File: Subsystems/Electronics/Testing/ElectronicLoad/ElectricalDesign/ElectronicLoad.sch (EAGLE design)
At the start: 74 parts, among them J1 USB, J2 Current Input, J3 Current Sense, J4 Voltage Sense, J5 SWD, Q1 IRFP4368PBF, Q2 SiRA20DP, Q3 SiRA20DP, Q4 IRFP4368PBF, SW1 Nice Knob, SW2 Nice Button, U1 STM32L476RGT, U2 AD8515, U3 FT230XQ, U4 INA199C1, U6 INA199C1, Y1 8MHz ±10ppm

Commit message: Update ElectronicLoad.sch
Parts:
- J6: value (none) -> FAN
- J7: value (none) -> 12 V Input
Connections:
- removed net N$2: U1A.PA11
- net FAN_SENSE: now also U1A.PA11
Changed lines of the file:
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@@
 <part name="SUPPLY56" library="CougsInSpace-PowerSymbols" deviceset="5.0V" device=""/>
 <part name="OFFSHEET11" library="CougsInSpace-Aesthetics" deviceset="OFF_SHEET-OUT" device=""/>
-<part name="J6" library="CougsInSpace-Connectors" deviceset="1X04" device="THT2.54-1X04-LOCK"/>
+<part name="J6" library="CougsInSpace-Connectors" deviceset="1X04" device="THT2.54-1X04-LOCK" value="FAN"/>
 <part name="OFFSHEET47" library="CougsInSpace-Aesthetics" deviceset="OFF_SHEET-OUT" device=""/>
 <part name="OFFSHEET49" library="CougsInSpace-Aesthetics" deviceset="OFF_SHEET-IN" device=""/>
@@
 <part name="SUPPLY67" library="CougsInSpace-PowerSymbols" deviceset="PGND" device=""/>
 <part name="OFFSHEET51" library="CougsInSpace-Aesthetics" deviceset="OFF_SHEET-OUT" device=""/>
-<part name="J7" library="CougsInSpace-Connectors" deviceset="BARREL" device="-2.1X5.5-R"/>
+<part name="J7" library="CougsInSpace-Connectors" deviceset="BARREL" device="-2.1X5.5-R" value="12 V Input"/>
 <part name="SUPPLY68" library="CougsInSpace-PowerSymbols" deviceset="12.0V" device=""/>
 <part name="SUPPLY69" library="CougsInSpace-PowerSymbols" deviceset="PGND" device=""/>
@@
 </segment>
 </net>
-<net name="N$2" class="0">
-<segment>
-<pinref part="U1" gate="A" pin="PA11"/>
-<wire x1="33.02" y1="66.04" x2="50.8" y2="66.04" width="0.1524" layer="91"/>
-</segment>
-</net>
-<net name="FAN_SENSE" class="0">
-<segment>
-<wire x1="38.1" y1="66.04" x2="55.88" y2="66.04" width="0.1524" layer="91"/>
-<label x="35.56" y="66.04" size="1.778" layer="95"/>
-<label x="35.56" y="66.04" size="1.778" layer="95"/>
-</segment>
-</net>
 <net name="FAN_CONTROL" class="0">
 <segment>
@@
 <pinref part="J7" gate="G$1" pin="CENTER"/>
 <wire x1="172.72" y1="165.1" x2="167.64" y2="165.1" width="0.1524" layer="91"/>
+</segment>
+</net>
+<net name="FAN_SENSE" class="0">
+<segment>
+<pinref part="U1" gate="A" pin="PA11"/>
+<wire x1="33.02" y1="66.04" x2="55.88" y2="66.04" width="0.1524" layer="91"/>
+<label x="35.56" y="66.04" size="1.778" layer="95"/>
 </segment>
 </net>
@@
 </instance>
 <instance part="OFFSHEET16" gate="G$1" x="83.82" y="55.88" smashed="yes" rot="MR0"/>
-<instance part="OFFSHEET24" gate="G$1" x="210.82" y="48.26" smashed="yes" rot="MR0"/>
+<instance part="OFFSHEET24" gate="G$1" x="106.68" y="132.08" smashed="yes" rot="MR0"/>
 <instance part="J2" gate="G$1" x="144.78" y="142.24" smashed="yes">
 <attribute name="VALUE" x="145.415" y="138.43" size="1.778" layer="96" align="center"/>
@@
 <instance part="OFFSHEET49" gate="G$1" x="104.14" y="157.48" smashed="yes" rot="MR0"/>
 <instance part="OFFSHEET50" gate="G$1" x="104.14" y="154.94" smashed="yes" rot="MR0"/>
-<instance part="SUPPLY66" gate="G$1" x="96.52" y="162.56" smashed="yes">
-<attribute name="VALUE" x="96.52" y="166.116" size="1.27" layer="96" align="center"/>
-</instance>
-<instance part="SUPPLY67" gate="G$1" x="91.44" y="162.56" smashed="yes" rot="R90"/>
+<instance part="SUPPLY66" gate="G$1" x="88.9" y="162.56" smashed="yes">
+<attribute name="VALUE" x="88.9" y="166.116" size="1.27" layer="96" align="center"/>
+</instance>
+<instance part="SUPPLY67" gate="G$1" x="86.36" y="149.86" smashed="yes"/>
 </instances>
 <busses>
@@
 </segment>
 </net>
+<net name="12.0V" class="0">
+<segment>
+<pinref part="J6" gate="G$1" pin="2"/>
+<wire x1="81.28" y1="160.02" x2="88.9" y2="160.02" width="0.1524" layer="91"/>
+<pinref part="SUPPLY66" gate="G$1" pin="12.0V"/>
+<wire x1="88.9" y1="160.02" x2="88.9" y2="162.56" width="0.1524" layer="91"/>
+</segment>
+</net>
 <net name="FAN_SENSE" class="0">
 <segment>
@@
 </segment>
 </net>
-<net name="FAN_SENSE1" class="0">
-<segment>
-<wire x1="81.28" y1="154.94" x2="101.6" y2="154.94" width="0.1524" layer="91"/>
-</segment>
-</net>
 <net name="PGND" class="0">
 <segment>
 <pinref part="J6" gate="G$1" pin="1"/>
+<wire x1="81.28" y1="162.56" x2="86.36" y2="162.56" width="0.1524" layer="91"/>
 <pinref part="SUPPLY67" gate="G$1" pin="PGND"/>
-<wire x1="88.9" y1="162.56" x2="81.28" y2="162.56" width="0.1524" layer="91"/>
-</segment>
-</net>
-<net name="12.0V" class="0">
-<segment>
-<pinref part="J6" gate="G$1" pin="2"/>
-<wire x1="81.28" y1="160.02" x2="96.52" y2="160.02" width="0.1524" layer="91"/>
-<pinref part="SUPPLY66" gate="G$1" pin="12.0V"/>
-<wire x1="96.52" y1="160.02" x2="96.52" y2="162.56" width="0.1524" layer="91"/>
-</segment>
-</net>
+<wire x1="86.36" y1="162.56" x2="86.36" y2="152.4" width="0.1524" layer="91"/>
+</segment>
+</net>

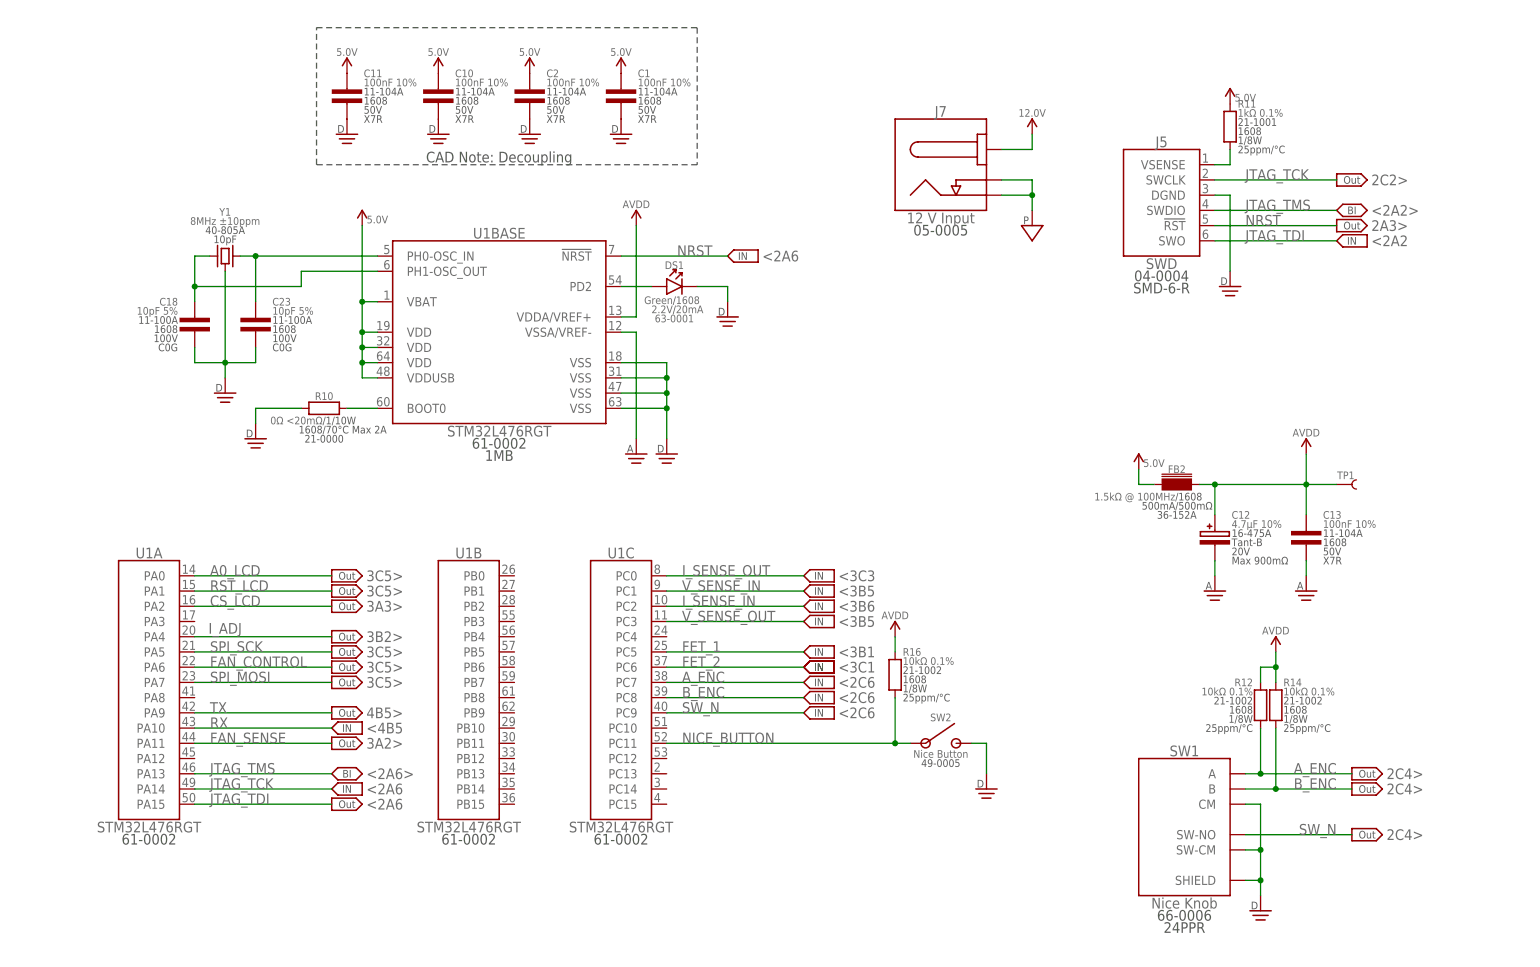
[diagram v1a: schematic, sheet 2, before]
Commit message: Added LDO, Fixed Formatting
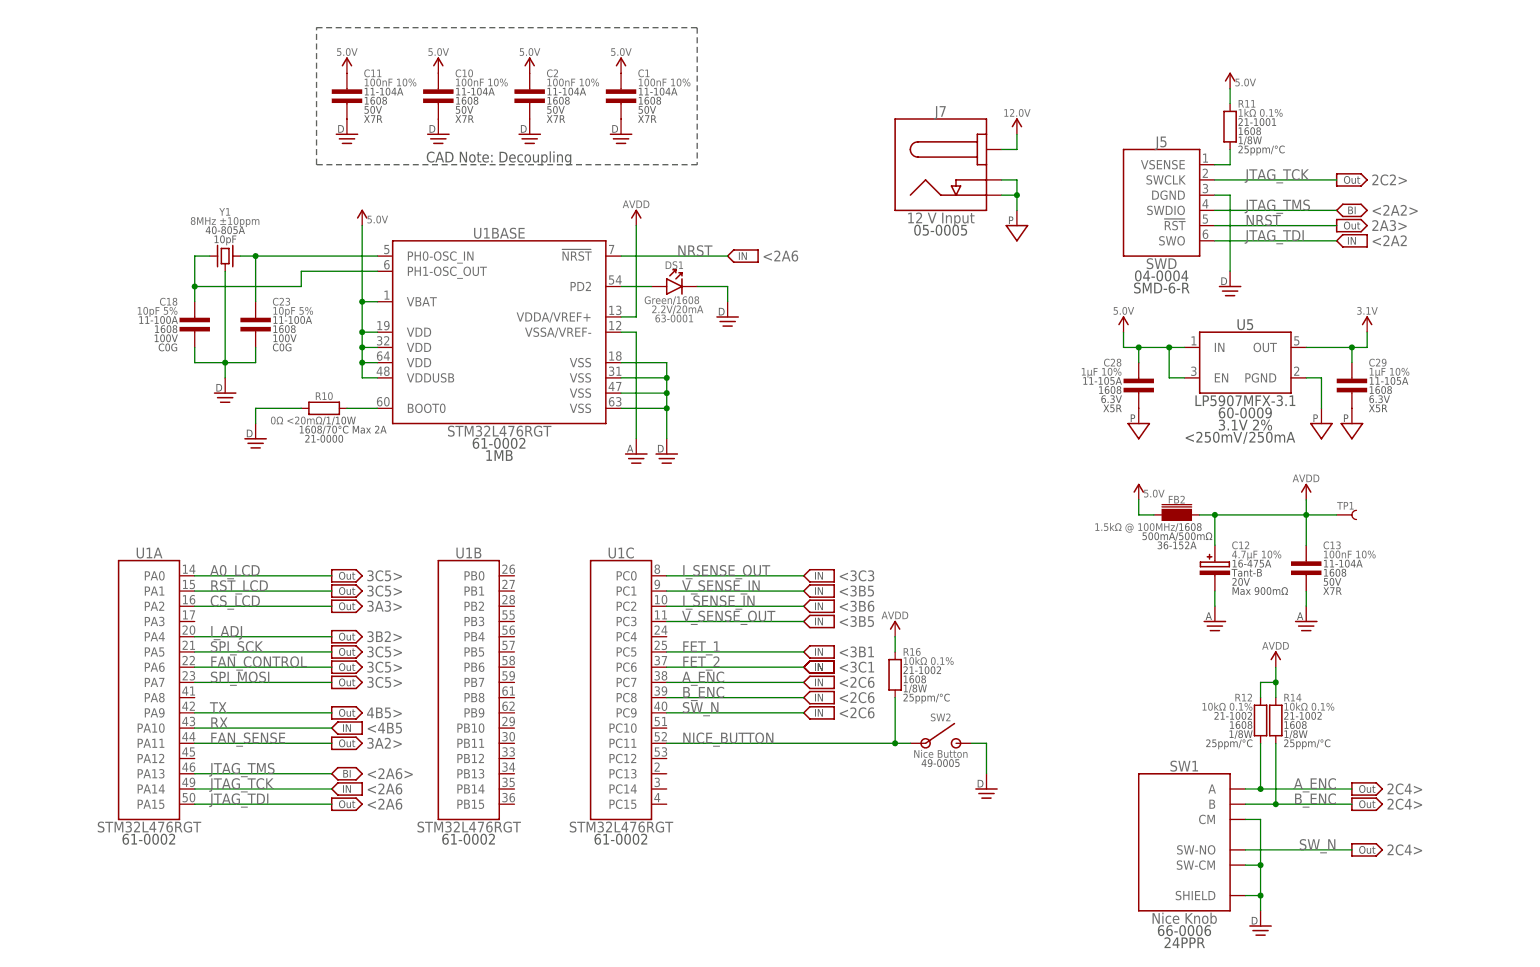
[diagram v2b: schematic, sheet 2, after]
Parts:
- added C28, C29: 1µF 10%, CougsInSpace-Capacitors:CAP-V-1UF-1608
- added R19: 60.4Ω 0.1%, CougsInSpace-Resistors:RES-H-60.4R-1608
- added U5: LP5907MFX-3.1, CougsInSpace-IC-Power:LDO-3.1-SOT23-5
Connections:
- net N$1 renamed OP_AMP_IN
- net N$3 renamed OSC_OUT
- net N$4 renamed OSC_IN
- new net 3.1V: B1.VDD, C29.1, U5.OUT
- new net LCD_LED: B1.LED+, R19.2
- net 5.0V: now also C28.1, R19.1, U5.EN, U5.IN
- net AVDD: no longer B1.LED+, B1.VDD
- net CBUS1: now also R15.2; no longer R15.1
- net PGND: now also C28.2, C29.2, U5.PGND
- net TXLED_C: now also R15.1; no longer R15.2
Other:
- moved on the sheet: C12, C13, C5, C9, FB2, R12, R13, R14, R15, RN1A, RN1B, RN1C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

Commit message: Fixed electronic load errors
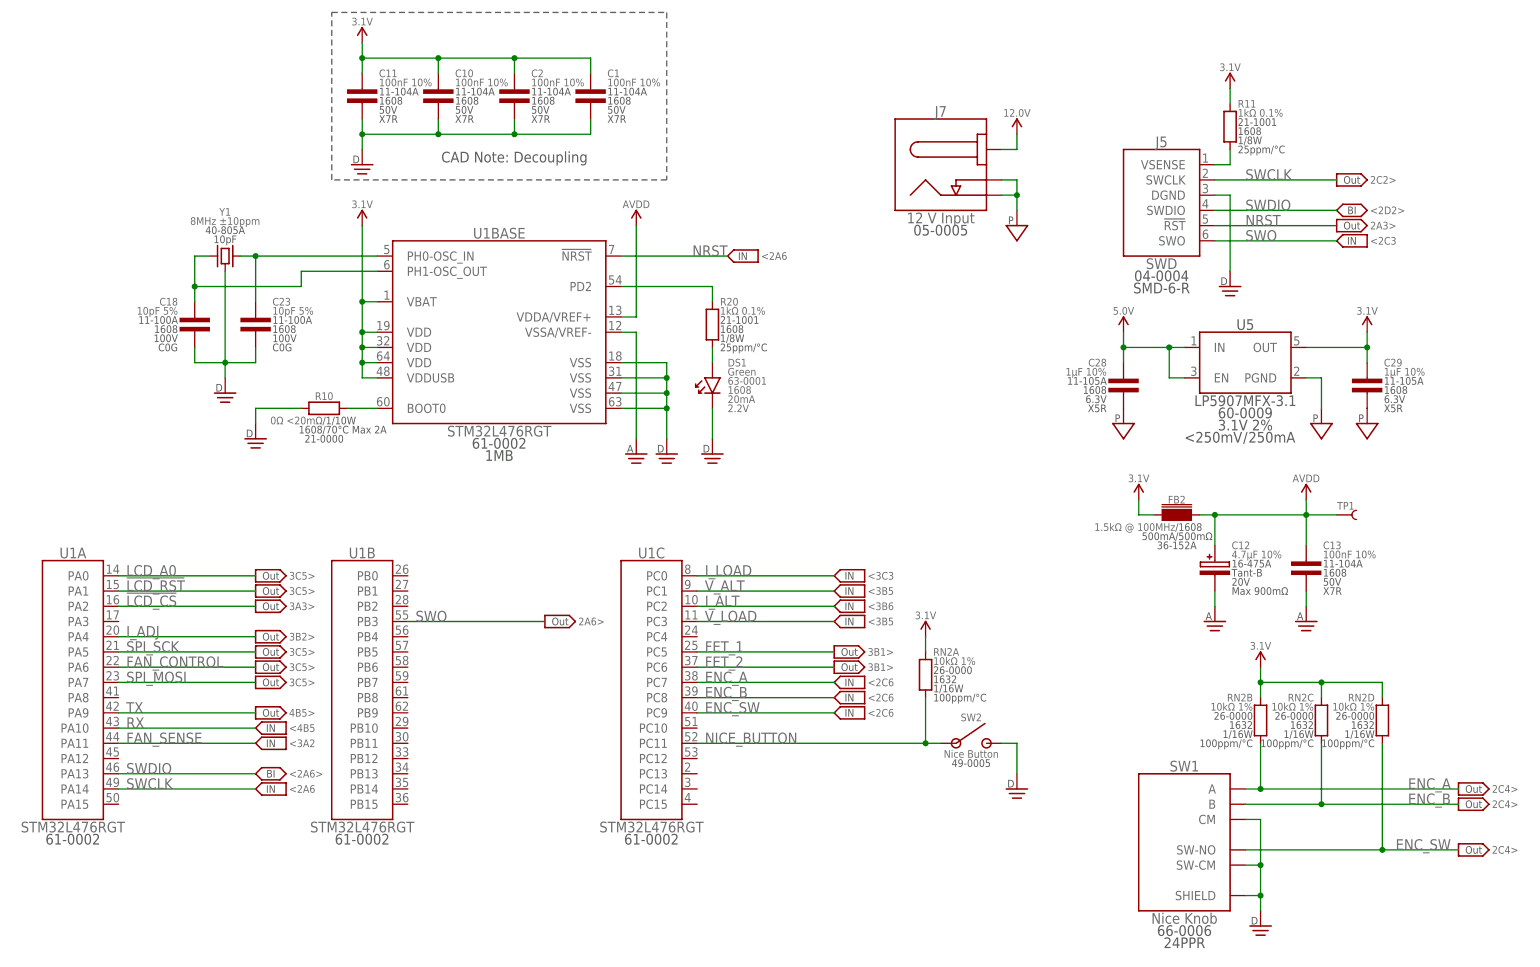
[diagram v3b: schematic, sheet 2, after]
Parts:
- added R20, R22, R23: 1kΩ 0.1%, CougsInSpace-Resistors:RES-V-1K-1608
- added R21: 0Ω <20mΩ, CougsInSpace-Resistors:RES-V-0-1608
- added R24: 10kΩ 0.1%, CougsInSpace-Resistors:RES-V-10K-1608
- added RN2: 10kΩ 1%, CougsInSpace-Resistors:RES-4-V-10K-1632
- DS1: device CougsInSpace-LEDs:LED-H-GRN-1608 -> CougsInSpace-LEDs:LED-V-GRN-1608
- J2: value Current Input -> Load
- J3: value Current Sense -> Alternate Current Sense
- R12, R14: value 10kΩ 0.1% -> 30kΩ 1%; device CougsInSpace-Resistors:RES-V-10K-1608 -> CougsInSpace-Resistors:RES-V-30K-1608
- R19: value 60.4Ω 0.1% -> 0Ω <20mΩ; device CougsInSpace-Resistors:RES-H-60.4R-1608 -> CougsInSpace-Resistors:RES-H-0-1608
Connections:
- net A0_LCD renamed LCD_A0
- net CS_LCD renamed !LCD_CS
- net I_IN renamed LOAD_INPUT+
- net I_SENSE_IN renamed I_ALT
- net I_SENSE_IN+ renamed I_ALT+
- net I_SENSE_IN- renamed I_ALT-
- net I_SENSE_OUT renamed I_LOAD
- net JTAG_TCK renamed SWCLK
- net JTAG_TMS renamed SWDIO
- net RST_LCD renamed !LCD_RST
- removed net 3.3V: C3.1, DS3.A, DS5.A, R7.1, RN1A.2, RN1B.2, RN1C.2, RN1D.2, U3.3V3OUT, U3.VCCIO
- removed net A_ENC: R12.1, SW1.A, U1C.PC7
- removed net B_ENC: R14.1, SW1.B, U1C.PC8
- removed net I_OUT: J2.2, R6.1
- removed net JTAG_TDI: J5.SWO, U1A.PA15
- removed net SW_N: SW1.SW-NO, U1C.PC9
- removed net USB5V_FILTERED: C6.1, C8.A, FB1.2, TP6.1, U3.VCC
- removed net V_SENSE_IN: J4.1, U1C.PC1
- removed net V_SENSE_OUT: J4.2, U1C.PC3
- new net ENC_A: RN2B.1, SW1.A, U1C.PC7
- new net ENC_B: RN2C.1, SW1.B, U1C.PC8
- new net ENC_SW: RN2D.1, SW1.SW-NO, U1C.PC9
- new net LOAD_INPUT-: J2.2, R22.2, R6.1
- new net SWO: J5.SWO, U1B.PB3
- new net TO_LED_ANODE: DS1.A, R20.1
- new net VSENSE_ALT: J4.1, R14.2
- new net VSENSE_GND: J4.3, R23.2
- new net VSENSE_LOAD: J4.2, R12.2
- new net V_ALT: R14.1, R24.2, U1C.PC1
- new net V_LOAD: R12.1, R16.2, U1C.PC3
- net 3.1V: now also C1.1, C10.1, C11.1, C2.1, C24.1, C26.1, C27.1, C3.1, DS3.A, DS5.A, FB2.1, R11.2, R19.1, R7.1, RN1A.2, RN1B.2, RN1C.2, RN1D.2, RN2A.2, RN2B.2, RN2C.2, RN2D.2, U1BASE.VBAT, U1BASE.VDD@1, U1BASE.VDD@2, U1BASE.VDD@3, U1BASE.VDDUSB, U3.VCCIO, U4.VDD, U6.VDD
- net 5.0V: now also C6.1, C8.A, FB1.2, TP6.1, U3.VCC; no longer C1.1, C10.1, C11.1, C2.1, C24.1, C26.1, FB2.1, R11.2, R19.1, U1BASE.VBAT, U1BASE.VDD@1, U1BASE.VDD@2, U1BASE.VDD@3, U1BASE.VDDUSB, U4.VDD, U6.VDD
- net AGND: now also R17.1
- net AVDD: no longer C27.1, R12.2, R14.2, R16.2
- net CBUS1: now also R15.1; no longer R15.2
- net CHASSIS: no longer R17.2
- net DGND: now also R16.1, R17.2, R21.2, R22.1, R23.1, R24.1; no longer J4.3, R17.1
- net NICE_BUTTON: now also RN2A.1; no longer R16.1
- net PGND: now also R21.1
- net TO_LED: now also R20.2; no longer DS1.A
- net TXLED_C: now also R15.2; no longer R15.1
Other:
- note added: "2A6>"
- note added: "3B1>"
- note added: "<2C3"
- note added: "<2D2>"
- note added: "<3A2"
- note added: "Page 1: Block Diagram Page 2: Microcontroller Page 3: Electronic Load, LCD Page 4: USB Transceiver"
- note removed: "3A2>"
- note removed: "3C3>"
- note removed: "<2A2"
- note removed: "<2A2>"
- note removed: "<3B1"
- note removed: "<3C1"
- note removed: "Page 1: Block Diagram Page 2: Microcontroller Page 3: Electronic Load, LCD Page 4: USB Tranceiver"
- moved on the sheet: C1, C11, C2, C26, C28, C29, J2, J3, J4, R13, R15, R17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

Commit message: Layout is done
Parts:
- added H1: AM4 Heatsink, CougsInSpace-Hardware:HEATSINK-AM4
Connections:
- net CHASSIS: now also H1.CHASSIS

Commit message: Finished board layout
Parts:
- added C30: 1µF 10%, CougsInSpace-Capacitors:CAP-V-1UF-1608
- added C31: 1µF 10%, CougsInSpace-Capacitors:CAP-V-1UF-B-1608
- added D1, D2: LTC4411, CougsInSpace-DiscreteSemi:LTC4411
- added R25: 10kΩ 0.1%, CougsInSpace-Resistors:RES-V-10K-1608
- added R26: 30kΩ 1%, CougsInSpace-Resistors:RES-V-30K-1608
- added U7: TPS73250, CougsInSpace-IC-Power:LDO-FB-5.0-SOT23-5
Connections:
- new net N$1: C30.2, D1.IN, R25.2, U7.OUT
- new net N$2: C31.1, U7.EN, U7.IN
- new net N$3: C6.1, C8.A, D2.IN, FB1.2
- new net N$5: R25.1, R26.2, U7.FB
- net 5.0V: now also D1.OUT, D2.OUT; no longer C6.1, C8.A, FB1.2
- net DGND: now also C31.2, D1.GND, R26.1
- net PGND: now also C30.1, D2.GND, U7.PGND
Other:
- moved on the sheet: C28, C29, J7, U5

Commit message: Finished Board Layout
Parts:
- removed C30: 1µF 10%, CougsInSpace-Capacitors:CAP-V-1UF-1608
- removed C31: 1µF 10%, CougsInSpace-Capacitors:CAP-V-1UF-B-1608
- removed D1: LTC4411, CougsInSpace-DiscreteSemi:LTC4411
- removed J7: 12 V Input, CougsInSpace-Connectors:BARREL-2.1X5.5-R
- removed R25: 10kΩ 0.1%, CougsInSpace-Resistors:RES-V-10K-1608
- removed R26: 30kΩ 1%, CougsInSpace-Resistors:RES-V-30K-1608
- removed U7: TPS73250, CougsInSpace-IC-Power:LDO-FB-5.0-SOT23-5
- added C32: 1µF 10%, CougsInSpace-Capacitors:CAP-V-1UF-1608
- added C33: 1µF 10%, CougsInSpace-Capacitors:CAP-V-1UF-B-1608
- added D3: LTC4411, CougsInSpace-DiscreteSemi:LTC4411
- added J8: 12 V Input, CougsInSpace-Connectors:BARREL-2.1X5.5-R
- added R27: 10kΩ 0.1%, CougsInSpace-Resistors:RES-V-10K-1608
- added R28: 30kΩ 1%, CougsInSpace-Resistors:RES-V-30K-1608
- added U8: TPS73250, CougsInSpace-IC-Power:LDO-FB-5.0-SOT23-5
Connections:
- removed net N$1: C30.2, D1.IN, R25.2, U7.OUT
- removed net N$5: R25.1, R26.2, U7.FB
- new net N$4: C32.1, D3.IN, R27.2, U8.OUT
- new net N$7: R27.1, R28.2, U8.FB
- net 12.0V: now also J8.CENTER; no longer J7.CENTER
- net 5.0V: now also D3.OUT; no longer D1.OUT
- net DGND: no longer C31.2, D1.GND, R26.1
- net N$2: now also C33.1, U8.EN, U8.IN; no longer C31.1, U7.EN, U7.IN
- net PGND: now also C32.2, C33.2, D3.GND, J8.SLEEVE, J8.SW, R28.1, U8.PGND; no longer C30.1, J7.SLEEVE, J7.SW, U7.PGND
